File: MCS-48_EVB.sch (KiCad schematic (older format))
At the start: 6 parts

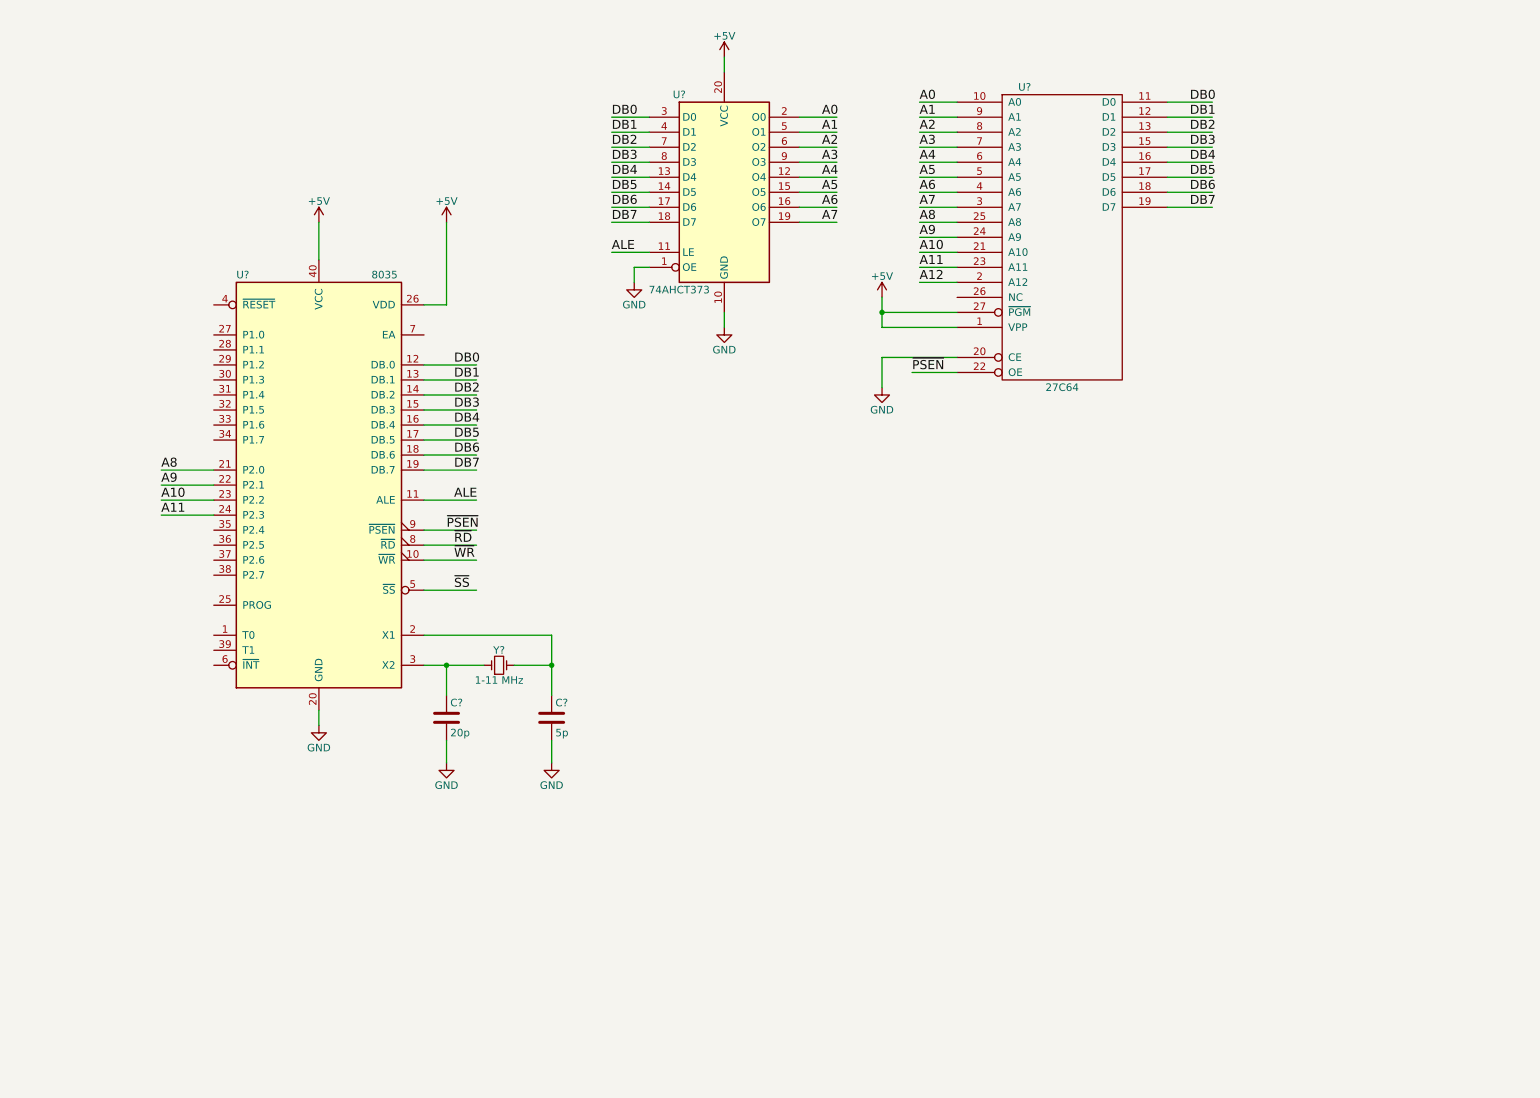
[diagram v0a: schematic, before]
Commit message: Added memories & expander
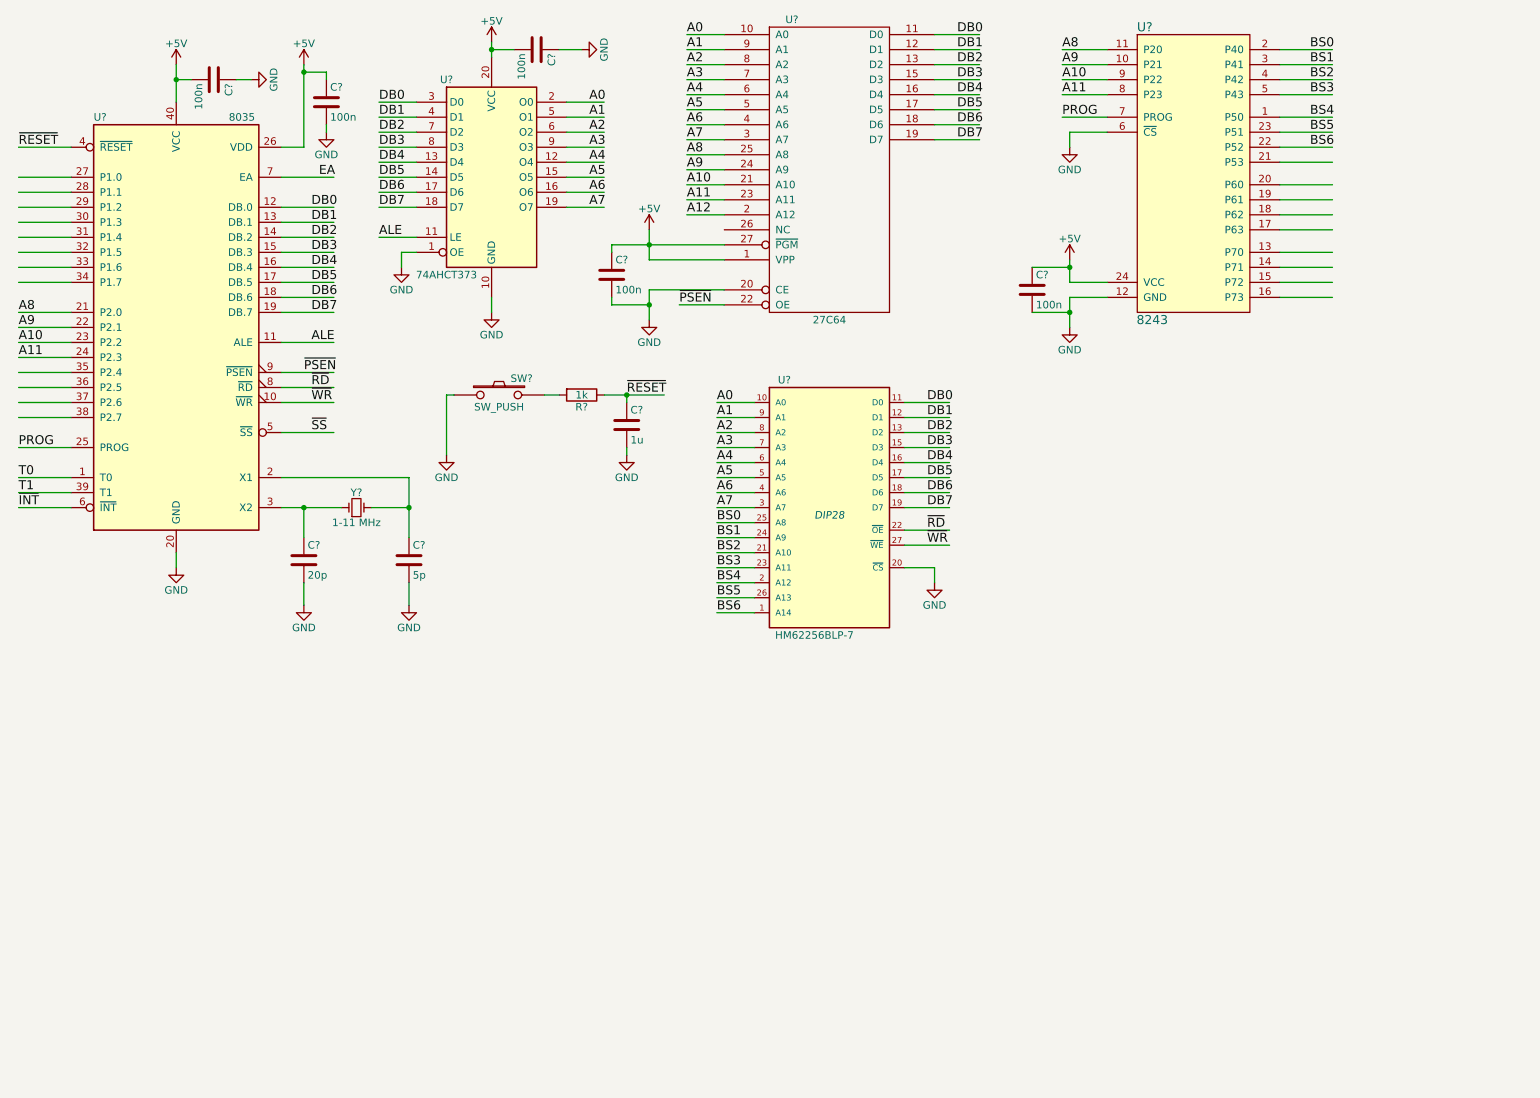
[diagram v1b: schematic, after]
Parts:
- added C? (x5): 100n, symbol C
- added C?: 1u, symbol C
- added R?: 1k, symbol R
- added SW?: SW_PUSH, symbol SW_PUSH
- added U?: 8243, Housings_DIP:DIP-24_W15.24mm_LongPads, symbol 8243
- added U?: HM62256BLP-7, DIP28, symbol HM62256BLP-7
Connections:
- net labels added: BS0, BS1, BS2, BS3, BS4, BS5, BS6, EA, PROG, T0, T1, ~INT, ~RESET
- wire segments 76 -> 166
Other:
- moved on the sheet: C?, U?, Y?

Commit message: Added RESET and EA circuits. Added MCS-48 docs.
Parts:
- added P? (x2): CONN_01X03, symbol CONN_01X03
- added R?: 22k, symbol R
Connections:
- wire segments 166 -> 177
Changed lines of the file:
@@
 	9150 1450 9500 1450
-Wire Wire Line
-	9150 1550 9500 1550
 Wire Wire Line
 	9150 1700 9500 1700
@@
 Text Label 4800 3100 0    60   ~ 0
 ~RESET
+$Comp
+L CONN_01X03 P?
+U 1 1 63B913D7
+P 9900 1100
+F 0 "P?" H 9900 1300 50  0000 C CNN
+F 1 "CONN_01X03" V 10000 1100 50  0000 C CNN
+F 2 "" H 9900 1100 50  0000 C CNN
+F 3 "" H 9900 1100 50  0000 C CNN
+	1    9900 1100
+	-1   0    0    1
+$EndComp
+Wire Wire Line
+	9150 1550 10150 1550
+Wire Wire Line
+	10150 1550 10150 1200
+Wire Wire Line
+	10100 1200 10200 1200
+Wire Wire Line
+	10100 1000 10150 1000
+Wire Wire Line
+	10150 1000 10150 850
+$Comp
+L GND #PWR?
+U 1 1 63B9189E
+P 10150 850
+F 0 "#PWR?" H 10150 600 50  0001 C CNN
+F 1 "GND" H 10150 700 50  0000 C CNN
+F 2 "" H 10150 850 50  0000 C CNN
+F 3 "" H 10150 850 50  0000 C CNN
+	1    10150 850
+	-1   0    0    1
+$EndComp
+Wire Wire Line
+	10100 1100 10350 1100
+Text Label 10200 1100 0    60   ~ 0
+A12
+$Comp
+L R R?
+U 1 1 63B919E3
+P 10350 1200
+F 0 "R?" V 10430 1200 50  0000 C CNN
+F 1 "22k" V 10350 1200 50  0000 C CNN
+F 2 "" V 10280 1200 50  0000 C CNN
+F 3 "" H 10350 1200 50  0000 C CNN
+	1    10350 1200
+	0    1    1    0
+$EndComp
+$Comp
+L GND #PWR?
+U 1 1 63B91AD9
+P 10600 1200
+F 0 "#PWR?" H 10600 950 50  0001 C CNN
+F 1 "GND" H 10600 1050 50  0000 C CNN
+F 2 "" H 10600 1200 50  0000 C CNN
+F 3 "" H 10600 1200 50  0000 C CNN
+	1    10600 1200
+	0    -1   -1   0
+$EndComp
+Connection ~ 10150 1200
+Wire Wire Line
+	10500 1200 10600 1200
+$Comp
+L CONN_01X03 P?
+U 1 1 63B929A8
+P 3950 4100
+F 0 "P?" H 3950 4300 50  0000 C CNN
+F 1 "CONN_01X03" V 4050 4100 50  0000 C CNN
+F 2 "" H 3950 4100 50  0000 C CNN
+F 3 "" H 3950 4100 50  0000 C CNN
+	1    3950 4100
+	-1   0    0    1
+$EndComp
+$Comp
+L GND #PWR?
+U 1 1 63B92B57
+P 4250 4300
+F 0 "#PWR?" H 4250 4050 50  0001 C CNN
+F 1 "GND" H 4250 4150 50  0000 C CNN
+F 2 "" H 4250 4300 50  0000 C CNN
+F 3 "" H 4250 4300 50  0000 C CNN
+	1    4250 4300
+	1    0    0    -1
+$EndComp
+$Comp
+L +5V #PWR?
+U 1 1 63B92B91
+P 4250 3900
+F 0 "#PWR?" H 4250 3750 50  0001 C CNN
+F 1 "+5V" H 4250 4040 50  0000 C CNN
+F 2 "" H 4250 3900 50  0000 C CNN
+F 3 "" H 4250 3900 50  0000 C CNN
+	1    4250 3900
+	1    0    0    -1
+$EndComp
+Wire Wire Line
+	4150 4000 4250 4000
+Wire Wire Line
+	4250 4000 4250 3900
+Wire Wire Line
+	4150 4200 4250 4200
+Wire Wire Line
+	4250 4200 4250 4300
+Wire Wire Line
+	4150 4100 4300 4100
+Text Label 4200 4100 0    60   ~ 0
+EA
 $EndSCHEMATC

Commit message: Added IC footprints
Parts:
- U?: footprint (none) -> Housings_DIP:DIP-40_W15.24mm_LongPads
- U?: footprint (none) -> Housings_DIP:DIP-20_W7.62mm_LongPads
- U?: footprint (none) -> Housings_DIP:DIP-28_W15.24mm_LongPads
- U?: footprint DIP28 -> Housings_DIP:DIP-28_W15.24mm_LongPads
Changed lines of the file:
@@
 F 0 "U?" H 1250 4050 50  0000 L CNN
 F 1 "8035" H 2150 4050 50  0000 L CNN
-F 2 "" H 1800 2850 50  0000 C CNN
+F 2 "Housings_DIP:DIP-40_W15.24mm_LongPads" H 1800 2850 50  0001 C CNN
 F 3 "" H 1800 2850 50  0000 C CNN
 	1    1800 2650
@@
 F 0 "U?" H 3600 2300 50  0000 C CNN
 F 1 "74AHCT373" H 3600 1000 50  0000 C CNN
-F 2 "" H 3900 1650 50  0001 C CNN
+F 2 "Housings_DIP:DIP-20_W7.62mm_LongPads" H 3900 1650 50  0001 C CNN
 F 3 "" H 3900 1650 50  0001 C CNN
 	1    3900 1650
@@
 F 0 "U?" H 5900 2600 50  0000 C CNN
 F 1 "27C64" H 6150 600 50  0000 C CNN
-F 2 "" H 6150 1600 50  0000 C CNN
+F 2 "Housings_DIP:DIP-28_W15.24mm_LongPads" H 6150 1600 50  0001 C CNN
 F 3 "" H 6150 1600 50  0000 C CNN
 	1    6150 1600
@@
 F 0 "U?" H 5850 4800 50  0000 C CNN
 F 1 "HM62256BLP-7" H 6050 3100 50  0000 C CNN
-F 2 "DIP28" H 6150 3900 50  0000 C CIN
+F 2 "Housings_DIP:DIP-28_W15.24mm_LongPads" H 6150 3900 50  0001 C CIN
 F 3 "" H 6150 3900 50  0000 C CNN
 	1    6150 3900

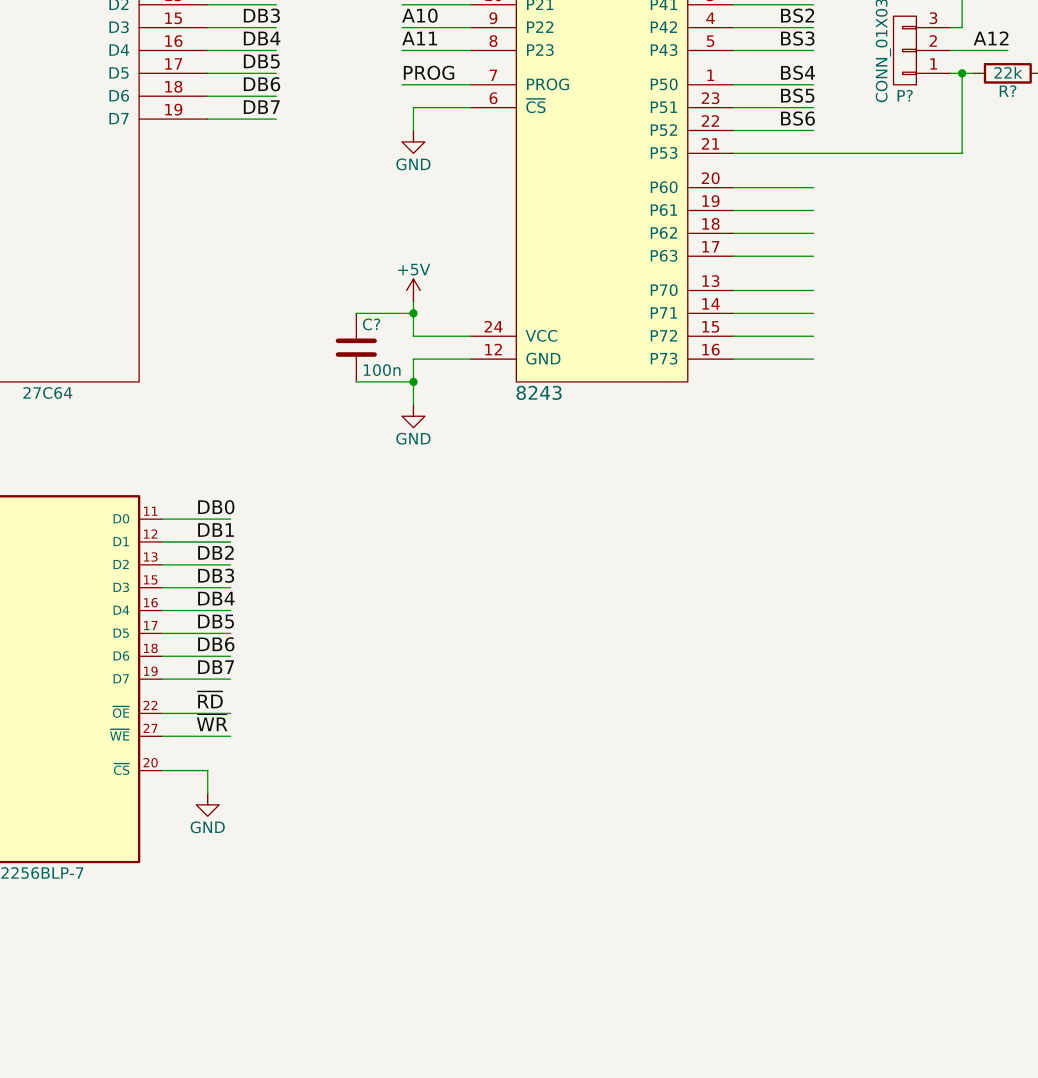
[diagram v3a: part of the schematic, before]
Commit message: Added 8155 expander
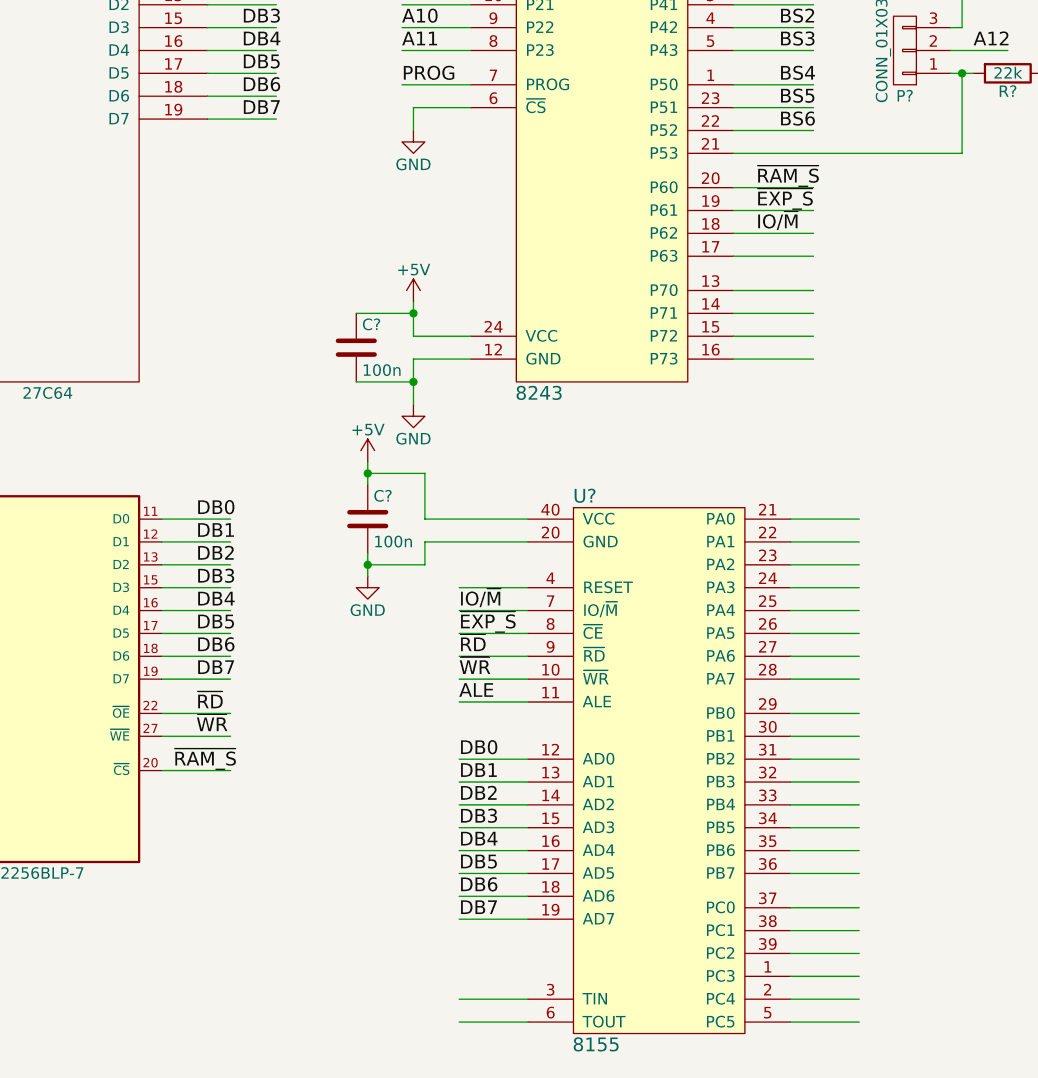
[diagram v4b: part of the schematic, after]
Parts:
- added C?: 100n, symbol C
- added U?: 8155, Housings_DIP:DIP-40_W15.24mm_LongPads, symbol 8155
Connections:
- net labels added: IO/~M, ~EXP_S, ~RAM_S
- wire segments 177 -> 222
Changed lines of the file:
@@
 LIBS:contrib
 LIBS:valves
+LIBS:MCS-48
 LIBS:MCS-48_EVB-cache
 EELAYER 25 0
@@
 Wire Wire Line
 	6650 4100 6950 4100
-$Comp
-L GND #PWR?
-U 1 1 63B8D3EE
-P 6850 4350
-F 0 "#PWR?" H 6850 4100 50  0001 C CNN
-F 1 "GND" H 6850 4200 50  0000 C CNN
-F 2 "" H 6850 4350 50  0000 C CNN
-F 3 "" H 6850 4350 50  0000 C CNN
-	1    6850 4350
-	1    0    0    -1
-$EndComp
-Wire Wire Line
-	6650 4250 6850 4250
-Wire Wire Line
-	6850 4250 6850 4350
+Wire Wire Line
+	6650 4250 6950 4250
 Text Label 6800 4100 0    60   ~ 0
 ~WR
@@
 Text Label 4200 4100 0    60   ~ 0
 EA
+Text Label 6700 4250 0    60   ~ 0
+~RAM_S
+Text Label 9250 1700 0    60   ~ 0
+~RAM_S
+$Comp
+L 8155 U?
+U 1 1 63B981E9
+P 8850 4450
+F 0 "U?" H 8500 5850 60  0000 C CNN
+F 1 "8155" H 8550 3450 60  0000 C CNN
+F 2 "Housings_DIP:DIP-40_W15.24mm_LongPads" H 8850 4450 60  0001 C CNN
+F 3 "" H 8850 4450 60  0001 C CNN
+	1    8850 4450
+	1    0    0    -1
+$EndComp
+$Comp
+L C C?
+U 1 1 63B98328
+P 7550 3150
+F 0 "C?" H 7575 3250 50  0000 L CNN
+F 1 "100n" H 7575 3050 50  0000 L CNN
+F 2 "" H 7588 3000 50  0000 C CNN
+F 3 "" H 7550 3150 50  0000 C CNN
+	1    7550 3150
+	1    0    0    -1
+$EndComp
+$Comp
+L +5V #PWR?
+U 1 1 63B983C7
+P 7550 2900
+F 0 "#PWR?" H 7550 2750 50  0001 C CNN
+F 1 "+5V" H 7550 3040 50  0000 C CNN
+F 2 "" H 7550 2900 50  0000 C CNN
+F 3 "" H 7550 2900 50  0000 C CNN
+	1    7550 2900
+	1    0    0    -1
+$EndComp
+$Comp
+L GND #PWR?
+U 1 1 63B98498
+P 7550 3400
+F 0 "#PWR?" H 7550 3150 50  0001 C CNN
+F 1 "GND" H 7550 3250 50  0000 C CNN
+F 2 "" H 7550 3400 50  0000 C CNN
+F 3 "" H 7550 3400 50  0000 C CNN
+	1    7550 3400
+	1    0    0    -1
+$EndComp
+Wire Wire Line
+	7550 2900 7550 3000
+Wire Wire Line
+	7550 3300 7550 3400
+Wire Wire Line
+	8250 3150 7800 3150
+Wire Wire Line
+	7800 3150 7800 2950
+Wire Wire Line
+	7800 2950 7550 2950
+Connection ~ 7550 2950
+Wire Wire Line
+	8250 3250 7800 3250
+Wire Wire Line
+	7800 3250 7800 3350
+Wire Wire Line
+	7800 3350 7550 3350
+Connection ~ 7550 3350
+Wire Wire Line
+	9400 3150 9700 3150
+Wire Wire Line
+	9400 3250 9700 3250
+Wire Wire Line
+	9400 3350 9700 3350
+Wire Wire Line
+	9400 3450 9700 3450
+Wire Wire Line
+	9400 3550 9700 3550
+Wire Wire Line
+	9400 3650 9700 3650
+Wire Wire Line
+	9400 3750 9700 3750
+Wire Wire Line
+	9400 3850 9700 3850
+Wire Wire Line
+	9400 4000 9700 4000
+Wire Wire Line
+	9400 4100 9700 4100
+Wire Wire Line
+	9400 4200 9700 4200
+Wire Wire Line
+	9400 4300 9700 4300
+Wire Wire Line
+	9400 4400 9700 4400
+Wire Wire Line
+	9400 4500 9700 4500
+Wire Wire Line
+	9400 4600 9700 4600
+Wire Wire Line
+	9400 4700 9700 4700
+Wire Wire Line
+	9400 4850 9700 4850
+Wire Wire Line
+	9400 4950 9700 4950
+Wire Wire Line
+	9400 5050 9700 5050
+Wire Wire Line
+	9400 5150 9700 5150
+Wire Wire Line
+	9400 5250 9700 5250
+Wire Wire Line
+	9400 5350 9700 5350
+Wire Wire Line
+	8250 3450 7950 3450
+Wire Wire Line
+	8250 3550 7950 3550
+Wire Wire Line
+	8250 3650 7950 3650
+Wire Wire Line
+	8250 3750 7950 3750
+Wire Wire Line
+	8250 3850 7950 3850
+Wire Wire Line
+	8250 3950 7950 3950
+Wire Wire Line
+	8250 4200 7950 4200
+Wire Wire Line
+	8250 4300 7950 4300
+Wire Wire Line
+	8250 4400 7950 4400
+Wire Wire Line
+	8250 4500 7950 4500
+Wire Wire Line
+	8250 4600 7950 4600
+Wire Wire Line
+	8250 4700 7950 4700
+Wire Wire Line
+	8250 4800 7950 4800
+Wire Wire Line
+	8250 4900 7950 4900
+Wire Wire Line
+	8250 5250 7950 5250
+Wire Wire Line
+	8250 5350 7950 5350
+Text Label 7950 3650 0    60   ~ 0
+~EXP_S
+Text Label 9250 1800 0    60   ~ 0
+~EXP_S
+Text Label 9250 1900 0    60   ~ 0
+IO/~M
+Text Label 7950 3550 0    60   ~ 0
+IO/~M
+Text Label 7950 3750 0    60   ~ 0
+~RD
+Text Label 7950 3850 0    60   ~ 0
+~WR
+Text Label 7950 3950 0    60   ~ 0
+ALE
+Text Label 7950 4200 0    60   ~ 0
+DB0
+Text Label 7950 4300 0    60   ~ 0
+DB1
+Text Label 7950 4400 0    60   ~ 0
+DB2
+Text Label 7950 4500 0    60   ~ 0
+DB3
+Text Label 7950 4600 0    60   ~ 0
+DB4
+Text Label 7950 4700 0    60   ~ 0
+DB5
+Text Label 7950 4800 0    60   ~ 0
+DB6
+Text Label 7950 4900 0    60   ~ 0
+DB7
 $EndSCHEMATC
